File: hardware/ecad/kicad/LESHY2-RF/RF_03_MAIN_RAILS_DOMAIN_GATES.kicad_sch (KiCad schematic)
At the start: 0 parts

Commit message: complete exact H2.3.1 RF power hierarchy
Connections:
- no-connect marks 0 -> 20
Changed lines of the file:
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@@
 	(generator_version "10.0")
 	(paper "A4")
+	(hierarchical_label "3V3_MAIN"
+		(shape bidirectional)
+		(at 20.32 20.32 0)
+		(effects (font (size 1.27 1.27)))
+	)
+	(wire
+		(pts (xy 20.32 20.32) (xy 25.40 20.32))
+		(stroke (width 0) (type default))
+	)
+	(no_connect (at 25.40 20.32)
+	)
+	(hierarchical_label "5V_EXT_PREPROTECT"
+		(shape bidirectional)
+		(at 20.32 25.40 0)
+		(effects (font (size 1.27 1.27)))
+	)
+	(wire
+		(pts (xy 20.32 25.40) (xy 25.40 25.40))
+		(stroke (width 0) (type default))
+	)
+	(no_connect (at 25.40 25.40)
+	)
+	(hierarchical_label "5V_U214_PROTECTED"
+		(shape bidirectional)
+		(at 20.32 30.48 0)
+		(effects (font (size 1.27 1.27)))
+	)
+	(wire
+		(pts (xy 20.32 30.48) (xy 25.40 30.48))
+		(stroke (width 0) (type default))
+	)
+	(no_connect (at 25.40 30.48)
+	)
+	(hierarchical_label "AON_BUCK_EN"
+		(shape bidirectional)
+		(at 20.32 35.56 0)
+		(effects (font (size 1.27 1.27)))
+	)
+	(wire
+		(pts (xy 20.32 35.56) (xy 25.40 35.56))
+		(stroke (width 0) (type default))
+	)
+	(no_connect (at 25.40 35.56)
+	)
+	(hierarchical_label "AON_PG_N"
+		(shape bidirectional)
+		(at 20.32 40.64 0)
+		(effects (font (size 1.27 1.27)))
+	)
+	(wire
+		(pts (xy 20.32 40.64) (xy 25.40 40.64))
+		(stroke (width 0) (type default))
+	)
+	(no_connect (at 25.40 40.64)
+	)
+	(hierarchical_label "AON_SAFE_3V3"
+		(shape bidirectional)
+		(at 20.32 45.72 0)
+		(effects (font (size 1.27 1.27)))
+	)
+	(wire
+		(pts (xy 20.32 45.72) (xy 25.40 45.72))
+		(stroke (width 0) (type default))
+	)
+	(no_connect (at 25.40 45.72)
+	)
+	(hierarchical_label "EV_N8_LORA_EXT"
+		(shape bidirectional)
+		(at 20.32 50.80 0)
+		(effects (font (size 1.27 1.27)))
+	)
+	(wire
+		(pts (xy 20.32 50.80) (xy 25.40 50.80))
+		(stroke (width 0) (type default))
+	)
+	(no_connect (at 25.40 50.80)
+	)
+	(hierarchical_label "EXT_ANY_5V_EN_SAFE"
+		(shape bidirectional)
+		(at 20.32 55.88 0)
+		(effects (font (size 1.27 1.27)))
+	)
+	(wire
+		(pts (xy 20.32 55.88) (xy 25.40 55.88))
+		(stroke (width 0) (type default))
+	)
+	(no_connect (at 25.40 55.88)
+	)
+	(hierarchical_label "EXT_ANY_5V_REQ"
+		(shape bidirectional)
+		(at 20.32 60.96 0)
+		(effects (font (size 1.27 1.27)))
+	)
+	(wire
+		(pts (xy 20.32 60.96) (xy 25.40 60.96))
+		(stroke (width 0) (type default))
+	)
+	(no_connect (at 25.40 60.96)
+	)
+	(hierarchical_label "NVDC_SYS"
+		(shape bidirectional)
+		(at 20.32 66.04 0)
+		(effects (font (size 1.27 1.27)))
+	)
+	(wire
+		(pts (xy 20.32 66.04) (xy 25.40 66.04))
+		(stroke (width 0) (type default))
+	)
+	(no_connect (at 25.40 66.04)
+	)
+	(hierarchical_label "POR_N"
+		(shape bidirectional)
+		(at 190.50 20.32 180)
+		(effects (font (size 1.27 1.27)) (justify right))
+	)
+	(wire
+		(pts (xy 190.50 20.32) (xy 185.42 20.32))
+		(stroke (width 0) (type default))
+	)
+	(no_connect (at 185.42 20.32)
+	)
+	(hierarchical_label "POWER_GROUND"
+		(shape bidirectional)
+		(at 190.50 25.40 180)
+		(effects (font (size 1.27 1.27)) (justify right))
+	)
+	(wire
+		(pts (xy 190.50 25.40) (xy 185.42 25.40))
+		(stroke (width 0) (type default))
+	)
+	(no_connect (at 185.42 25.40)
+	)
+	(hierarchical_label "POWER_ZONE_TEMP_ADC"
+		(shape bidirectional)
+		(at 190.50 30.48 180)
+		(effects (font (size 1.27 1.27)) (justify right))
+	)
+	(wire
+		(pts (xy 190.50 30.48) (xy 185.42 30.48))
+		(stroke (width 0) (type default))
+	)
+	(no_connect (at 185.42 30.48)
+	)
+	(hierarchical_label "RF_ZONE_TEMP_ADC"
+		(shape bidirectional)
+		(at 190.50 35.56 180)
+		(effects (font (size 1.27 1.27)) (justify right))
+	)
+	(wire
+		(pts (xy 190.50 35.56) (xy 185.42 35.56))
+		(stroke (width 0) (type default))
+	)
+	(no_connect (at 185.42 35.56)
+	)
+	(hierarchical_label "SAFETY_GROUND"
+		(shape bidirectional)
+		(at 190.50 40.64 180)
+		(effects (font (size 1.27 1.27)) (justify right))
+	)
+	(wire
+		(pts (xy 190.50 40.64) (xy 185.42 40.64))
+		(stroke (width 0) (type default))
+	)
+	(no_connect (at 185.42 40.64)
+	)
+	(hierarchical_label "U214_5V_EN_SAFE"
+		(shape bidirectional)
+		(at 190.50 45.72 180)
+		(effects (font (size 1.27 1.27)) (justify right))
+	)
+	(wire
+		(pts (xy 190.50 45.72) (xy 185.42 45.72))
+		(stroke (width 0) (type default))
+	)
+	(no_connect (at 185.42 45.72)
+	)
+	(hierarchical_label "U214_5V_REQ"
+		(shape bidirectional)
+		(at 190.50 50.80 180)
+		(effects (font (size 1.27 1.27)) (justify right))
+	)
+	(wire
+		(pts (xy 190.50 50.80) (xy 185.42 50.80))
+		(stroke (width 0) (type default))
+	)
+	(no_connect (at 185.42 50.80)
+	)
+	(hierarchical_label "U214_PIN5_PROFILE"
+		(shape bidirectional)
+		(at 190.50 55.88 180)
+		(effects (font (size 1.27 1.27)) (justify right))
+	)
+	(wire
+		(pts (xy 190.50 55.88) (xy 185.42 55.88))
+		(stroke (width 0) (type default))
+	)
+	(no_connect (at 185.42 55.88)
+	)
+	(hierarchical_label "UNIT_5V_EN_SAFE"
+		(shape bidirectional)
+		(at 190.50 60.96 180)
+		(effects (font (size 1.27 1.27)) (justify right))
+	)
+	(wire
+		(pts (xy 190.50 60.96) (xy 185.42 60.96))
+		(stroke (width 0) (type default))
+	)
+	(no_connect (at 185.42 60.96)
+	)
+	(hierarchical_label "UNIT_5V_REQ"
+		(shape bidirectional)
+		(at 190.50 66.04 180)
+		(effects (font (size 1.27 1.27)) (justify right))
+	)
+	(wire
+		(pts (xy 190.50 66.04) (xy 185.42 66.04))
+		(stroke (width 0) (type default))
+	)
+	(no_connect (at 185.42 66.04)
+	)
 	(sheet_instances
 		(path "/"

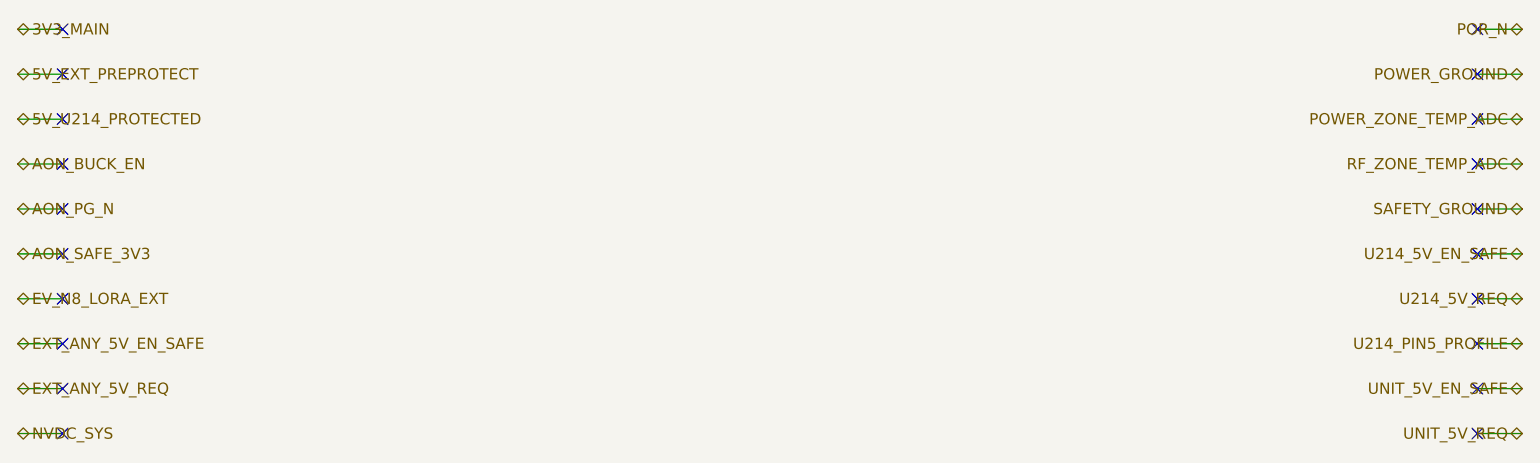
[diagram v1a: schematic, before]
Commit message: complete exact H2.3.2 USB PD charging
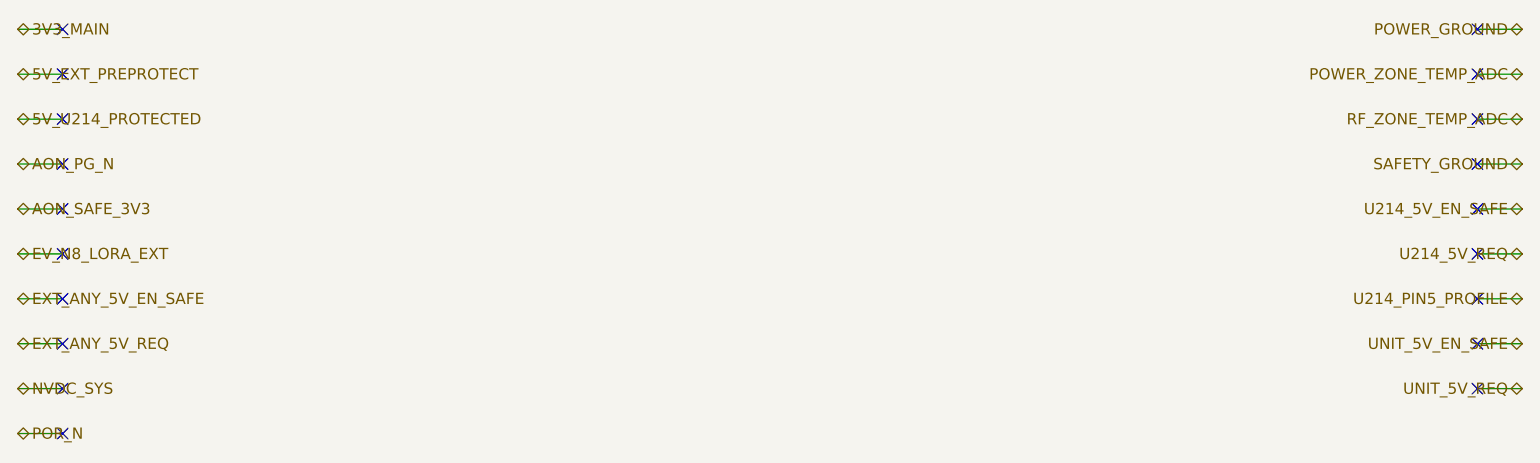
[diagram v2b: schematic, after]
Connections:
- no-connect marks 20 -> 19
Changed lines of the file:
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@@
 	(no_connect (at 25.40 30.48)
 	)
-	(hierarchical_label "AON_BUCK_EN"
+	(hierarchical_label "AON_PG_N"
 		(shape bidirectional)
 		(at 20.32 35.56 0)
@@
 	(no_connect (at 25.40 35.56)
 	)
-	(hierarchical_label "AON_PG_N"
+	(hierarchical_label "AON_SAFE_3V3"
 		(shape bidirectional)
 		(at 20.32 40.64 0)
@@
 	(no_connect (at 25.40 40.64)
 	)
-	(hierarchical_label "AON_SAFE_3V3"
+	(hierarchical_label "EV_N8_LORA_EXT"
 		(shape bidirectional)
 		(at 20.32 45.72 0)
@@
 	(no_connect (at 25.40 45.72)
 	)
-	(hierarchical_label "EV_N8_LORA_EXT"
+	(hierarchical_label "EXT_ANY_5V_EN_SAFE"
 		(shape bidirectional)
 		(at 20.32 50.80 0)
@@
 	(no_connect (at 25.40 50.80)
 	)
-	(hierarchical_label "EXT_ANY_5V_EN_SAFE"
+	(hierarchical_label "EXT_ANY_5V_REQ"
 		(shape bidirectional)
 		(at 20.32 55.88 0)
@@
 	(no_connect (at 25.40 55.88)
 	)
-	(hierarchical_label "EXT_ANY_5V_REQ"
+	(hierarchical_label "NVDC_SYS"
 		(shape bidirectional)
 		(at 20.32 60.96 0)
@@
 	(no_connect (at 25.40 60.96)
 	)
-	(hierarchical_label "NVDC_SYS"
+	(hierarchical_label "POR_N"
 		(shape bidirectional)
 		(at 20.32 66.04 0)
@@
 	(no_connect (at 25.40 66.04)
 	)
-	(hierarchical_label "POR_N"
+	(hierarchical_label "POWER_GROUND"
 		(shape bidirectional)
 		(at 190.50 20.32 180)
@@
 	(no_connect (at 185.42 20.32)
 	)
-	(hierarchical_label "POWER_GROUND"
+	(hierarchical_label "POWER_ZONE_TEMP_ADC"
 		(shape bidirectional)
 		(at 190.50 25.40 180)
@@
 	(no_connect (at 185.42 25.40)
 	)
-	(hierarchical_label "POWER_ZONE_TEMP_ADC"
+	(hierarchical_label "RF_ZONE_TEMP_ADC"
 		(shape bidirectional)
 		(at 190.50 30.48 180)
@@
 	(no_connect (at 185.42 30.48)
 	)
-	(hierarchical_label "RF_ZONE_TEMP_ADC"
+	(hierarchical_label "SAFETY_GROUND"
 		(shape bidirectional)
 		(at 190.50 35.56 180)
@@
 	(no_connect (at 185.42 35.56)
 	)
-	(hierarchical_label "SAFETY_GROUND"
+	(hierarchical_label "U214_5V_EN_SAFE"
 		(shape bidirectional)
 		(at 190.50 40.64 180)
@@
 	(no_connect (at 185.42 40.64)
 	)
-	(hierarchical_label "U214_5V_EN_SAFE"
+	(hierarchical_label "U214_5V_REQ"
 		(shape bidirectional)
 		(at 190.50 45.72 180)
@@
 	(no_connect (at 185.42 45.72)
 	)
-	(hierarchical_label "U214_5V_REQ"
+	(hierarchical_label "U214_PIN5_PROFILE"
 		(shape bidirectional)
 		(at 190.50 50.80 180)
@@
 	(no_connect (at 185.42 50.80)
 	)
-	(hierarchical_label "U214_PIN5_PROFILE"
+	(hierarchical_label "UNIT_5V_EN_SAFE"
 		(shape bidirectional)
 		(at 190.50 55.88 180)
@@
 	(no_connect (at 185.42 55.88)
 	)
-	(hierarchical_label "UNIT_5V_EN_SAFE"
+	(hierarchical_label "UNIT_5V_REQ"
 		(shape bidirectional)
 		(at 190.50 60.96 180)
@@
 	(no_connect (at 185.42 60.96)
 	)
-	(hierarchical_label "UNIT_5V_REQ"
-		(shape bidirectional)
-		(at 190.50 66.04 180)
-		(effects (font (size 1.27 1.27)) (justify right))
-	)
-	(wire
-		(pts (xy 190.50 66.04) (xy 185.42 66.04))
-		(stroke (width 0) (type default))
-	)
-	(no_connect (at 185.42 66.04)
-	)
 	(sheet_instances

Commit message: complete exact H2.3.4 power rails
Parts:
- added C1: TDK C1005X7R1H104K050BB, Capacitor_SMD:C_0402_1005Metric, symbol Leshy2:RF03_EXT_REQUEST_OR_BYPASS
- added C10: Murata GRM32ER71E226KE15L, Capacitor_SMD:C_1210_3225Metric, symbol Leshy2:RF03_MAIN_OUTPUT_CAP0
- added C11: Murata GRM32ER71E226KE15L, Capacitor_SMD:C_1210_3225Metric, symbol Leshy2:RF03_MAIN_OUTPUT_CAP1
- added C12: Murata GRM155R71H472KA01D, Capacitor_SMD:C_0402_1005Metric, symbol Leshy2:RF03_MAIN_EFUSE_DVDT_CAP
- added C13: Murata GRM1555C1H121JA01D, Capacitor_SMD:C_0402_1005Metric, symbol Leshy2:RF03_MAIN_EFUSE_ITIMER_CAP
- added C14: Murata GRM188R60J106ME47D, Capacitor_SMD:C_0603_1608Metric, symbol Leshy2:RF03_MAIN_EFUSE_OUTPUT_CAP
- added C15: Murata GRM32ER71E226KE15L, Capacitor_SMD:C_1210_3225Metric, symbol Leshy2:RF03_EXT_BUCK_INPUT_CAP
- added C16: TDK C1005X7R1H104K050BB, Capacitor_SMD:C_0402_1005Metric, symbol Leshy2:RF03_EXT_BUCK_HF_INPUT_CAP
- added C17: KEMET C0402C330J5GACTU, Capacitor_SMD:C_0402_1005Metric, symbol Leshy2:RF03_EXT_BUCK_FF_CAP
- added C18: Murata GRM32ER71E226KE15L, Capacitor_SMD:C_1210_3225Metric, symbol Leshy2:RF03_EXT_BUCK_OUTPUT_CAP0
- added C19: Murata GRM32ER71E226KE15L, Capacitor_SMD:C_1210_3225Metric, symbol Leshy2:RF03_EXT_BUCK_OUTPUT_CAP1
- added C2: TDK C1005X7R1H104K050BB, Capacitor_SMD:C_0402_1005Metric, symbol Leshy2:RF03_EXT_BRANCH_GATE_BYPASS
- added C20: Murata GRM155R71H472KA01D, Capacitor_SMD:C_0402_1005Metric, symbol Leshy2:RF03_EXT_DVDT_CAP
- added C21: Murata GRM188R71E224KA88D, Capacitor_SMD:C_0603_1608Metric, symbol Leshy2:RF03_EXT_ITIMER_CAP
- added C22: Murata GRM21BR71E225KE11L, Capacitor_SMD:C_0805_2012Metric, symbol Leshy2:RF03_EXT_INPUT_CAP
- added C23: Murata GRM21BR71E225KE11L, Capacitor_SMD:C_0805_2012Metric, symbol Leshy2:RF03_EXT_OUTPUT_CAP
- added C24: TDK C1005X7R1H104K050BB, Capacitor_SMD:C_0402_1005Metric, symbol Leshy2:RF03_POWER_ZONE_TEMP_FILTER
- added C25: TDK C1005X7R1H104K050BB, Capacitor_SMD:C_0402_1005Metric, symbol Leshy2:RF03_RF_ZONE_TEMP_FILTER
- added C26: TDK C1005X7R1H104K050BB, Capacitor_SMD:C_0402_1005Metric, symbol Leshy2:RF03_EXT_EVIDENCE_BUFFER_BYPASS
- added C3: TDK CGA5L1X7R1E475K160AC, Capacitor_SMD:C_1206_3216Metric, symbol Leshy2:RF03_AON_INPUT_CAP
- added C4: Murata GRM31CR71A226KE15L, Capacitor_SMD:C_1206_3216Metric, symbol Leshy2:RF03_AON_OUTPUT_CAP
- added C5: TDK C1005X7R1H104K050BB, Capacitor_SMD:C_0402_1005Metric, symbol Leshy2:RF03_AON_EFUSE_INPUT_CAP
- added C6: Murata GRM188R60J106ME47D, Capacitor_SMD:C_0603_1608Metric, symbol Leshy2:RF03_AON_EFUSE_OUTPUT_CAP
- added C7: Murata GRM32ER71E226KE15L, Capacitor_SMD:C_1210_3225Metric, symbol Leshy2:RF03_MAIN_INPUT_CAP
- added C8: TDK C1005X7R1H104K050BB, Capacitor_SMD:C_0402_1005Metric, symbol Leshy2:RF03_MAIN_HF_INPUT_CAP
- added C9: KEMET C0402C330J5GACTU, Capacitor_SMD:C_0402_1005Metric, symbol Leshy2:RF03_MAIN_FF_CAP
- added L1: Sunlord WPN201612H2R2MT, Inductor_SMD:L_Murata_LQH2MCNxxxx02_2.0x1.6mm, symbol Leshy2:RF03_AON_INDUCTOR
- added L2: Sunlord MWSA0503S-3R3MT, Inductor_SMD:L_Sunlord_MWSA0503S, symbol Leshy2:RF03_MAIN_INDUCTOR
- added L3: Sunlord MWSA0503S-4R7MT, Inductor_SMD:L_Sunlord_MWSA0503S, symbol Leshy2:RF03_EXT_INDUCTOR
- added Q1: Diodes Incorporated MMBT3904-7-F, Package_TO_SOT_SMD:SOT-23, symbol Leshy2:RF03_EXT_PG_QUALIFIER
- added R1: Yageo RC0402FR-0710KL, Resistor_SMD:R_0402_1005Metric, symbol Leshy2:RF03_EXT_ANY_REQ_PULLDOWN
- added R10: Yageo RT0402BRD07191KL, Resistor_SMD:R_0402_1005Metric, symbol Leshy2:RF03_MAIN_EFUSE_OVLO_TOP
- added R11: Yageo RT0402BRD07100KL, Resistor_SMD:R_0402_1005Metric, symbol Leshy2:RF03_MAIN_EFUSE_OVLO_BOTTOM
- added R12: Yageo RC0402FR-0745K3L, Resistor_SMD:R_0402_1005Metric, symbol Leshy2:RF03_MAIN_EFUSE_PG_TOP
- added R13: Yageo RC0402FR-0730KL, Resistor_SMD:R_0402_1005Metric, symbol Leshy2:RF03_MAIN_EFUSE_PG_BOTTOM
- added R14: Yageo RC0402FR-07100KL, Resistor_SMD:R_0402_1005Metric, symbol Leshy2:RF03_MAIN_EN_PULLDOWN
- added R15: Yageo RC0402FR-07220KL, Resistor_SMD:R_0402_1005Metric, symbol Leshy2:RF03_EXT_BUCK_FB_TOP
- added R16: Yageo RC0402FR-0730KL, Resistor_SMD:R_0402_1005Metric, symbol Leshy2:RF03_EXT_BUCK_FB_BOTTOM
- added R17: Yageo RC0402FR-0710KL, Resistor_SMD:R_0402_1005Metric, symbol Leshy2:RF03_EXT_EN_PULLDOWN
- added R18: Yageo RC0402FR-0710KL, Resistor_SMD:R_0402_1005Metric, symbol Leshy2:RF03_EXT_PG_PULLUP
- added R19: Yageo RC0402FR-0768KL, Resistor_SMD:R_0402_1005Metric, symbol Leshy2:RF03_EXT_PG_BASE_RES
- added R2: Yageo RC0402FR-0742K2L, Resistor_SMD:R_0402_1005Metric, symbol Leshy2:RF03_AON_MODE_RES
- added R20: Yageo RC0402FR-072K21L, Resistor_SMD:R_0402_1005Metric, symbol Leshy2:RF03_EXT_RILM
- added R21: Yageo RC0402FR-07169KL, Resistor_SMD:R_0402_1005Metric, symbol Leshy2:RF03_EXT_OVLO_TOP
- added R22: Yageo RC0402FR-0747KL, Resistor_SMD:R_0402_1005Metric, symbol Leshy2:RF03_EXT_OVLO_BOTTOM
- added R23: Yageo RC0603FR-071KL, Resistor_SMD:R_0603_1608Metric, symbol Leshy2:RF03_EXT_BLEEDER
- added R24: Yageo RC0402FR-0710KL, Resistor_SMD:R_0402_1005Metric, symbol Leshy2:RF03_POWER_ZONE_TEMP_PULLUP
- added R25: Yageo RC0402FR-0710KL, Resistor_SMD:R_0402_1005Metric, symbol Leshy2:RF03_RF_ZONE_TEMP_PULLUP
- added R26: Yageo RC0402FR-071KL, Resistor_SMD:R_0402_1005Metric, symbol Leshy2:RF03_EXT_EVIDENCE_INPUT_SERIES
- added R27: Yageo RC0402FR-0710KL, Resistor_SMD:R_0402_1005Metric, symbol Leshy2:RF03_EXT_EVIDENCE_INPUT_PULLUP
- added R28: Yageo RC0402FR-0710KL, Resistor_SMD:R_0402_1005Metric, symbol Leshy2:RF03_EXT_EVIDENCE_OUTPUT_PULLUP
- added R3: Yageo RC0402FR-07240KL, Resistor_SMD:R_0402_1005Metric, symbol Leshy2:RF03_AON_EFUSE_RILIM
- added R4: Yageo RC0402FR-07196KL, Resistor_SMD:R_0402_1005Metric, symbol Leshy2:RF03_AON_EFUSE_OVLO_TOP
- added R5: Yageo RC0402FR-07100KL, Resistor_SMD:R_0402_1005Metric, symbol Leshy2:RF03_AON_EFUSE_OVLO_BOTTOM
- added R6: Yageo RC0402FR-0747KL, Resistor_SMD:R_0402_1005Metric, symbol Leshy2:RF03_AON_PG_PULLUP
- added R7: Yageo RC0402FR-0745K3L, Resistor_SMD:R_0402_1005Metric, symbol Leshy2:RF03_MAIN_FB_TOP
- added R8: Yageo RC0402FR-0710KL, Resistor_SMD:R_0402_1005Metric, symbol Leshy2:RF03_MAIN_FB_BOTTOM
- added R9: Yageo RC0402FR-071K65L, Resistor_SMD:R_0402_1005Metric, symbol Leshy2:RF03_MAIN_EFUSE_RILM
- added RT1: TDK B57332V5103F360, Resistor_SMD:R_0603_1608Metric, symbol Leshy2:RF03_POWER_ZONE_NTC
- added RT2: TDK B57332V5103F360, Resistor_SMD:R_0603_1608Metric, symbol Leshy2:RF03_RF_ZONE_NTC
- added U1: 74LVC1G32GV,125, Package_TO_SOT_SMD:SC-74A-5_1.55x2.9mm_P0.95mm, symbol Leshy2:RF03_EXT_REQUEST_OR
- added U2: Texas Instruments SN74LVC2G08DCUR, Package_SO:VSSOP-8_2.3x2mm_P0.5mm, symbol Leshy2:RF03_EXT_BRANCH_GATE
- added U3: Texas Instruments TPS629203DRLR, Leshy2:TI-DRL0008A-SOT-5X3-8, symbol Leshy2:RF03_AON_BUCK
- added U4: Texas Instruments TPS25961DRVR, Package_SON:WSON-6-1EP_2x2mm_P0.65mm_EP1x1.6mm, symbol Leshy2:RF03_AON_EFUSE
- added U5: Texas Instruments TPS564252DRLR, Package_TO_SOT_SMD:Texas_R-PDSO-N6_DRL-6, symbol Leshy2:RF03_MAIN_BUCK
- added U6: Texas Instruments TPS25974LRPWR, Leshy2:TI-RPW0010A-VQFN-HR-10, symbol Leshy2:RF03_MAIN_EFUSE
- added U7: Texas Instruments TPS564252DRLR, Package_TO_SOT_SMD:Texas_R-PDSO-N6_DRL-6, symbol Leshy2:RF03_EXT_BUCK
- added U8: Texas Instruments TPS259470LRPWR, Leshy2:TI-RPW0010A-VQFN-HR-10, symbol Leshy2:RF03_EXT_EFUSE
- added U9: SN74LVC1G07DCKR, Package_TO_SOT_SMD:Texas_R-PDSO-G5_DCK-5, symbol Leshy2:RF03_EXT_EVIDENCE_BUFFER
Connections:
- net 3V3_MAIN: now also C14.1 (END_1), R12.1 (END_1), R18.1 (END_1), U6.6 (OUT)
- net 5V_EXT_PREPROTECT: now also C17.1 (END_1), C18.1 (END_1), C19.1 (END_1), C22.1 (END_1), L3.2 (END_2), R15.1 (END_1), R21.1 (END_1), U8.5 (IN)
- net 5V_U214_PROTECTED: now also C23.1 (END_1), R23.1 (END_1), U8.6 (OUT)
- net AON_PG_N: now also R6.2 (END_2), U3.2 (PG)
- net AON_SAFE_3V3: now also C1.1 (END_1), C2.1 (END_1), C26.1 (END_1), C6.1 (END_1), R24.1 (END_1), R25.1 (END_1), R27.1 (END_1), R28.1 (END_1), R6.1 (END_1), U1.5 (VCC), U2.8 (VCC), U4.1 (OUT), U9.5 (VCC)
- net EV_N8_LORA_EXT: now also R28.2 (END_2), U9.4 (Y)
- net EXT_ANY_5V_EN_SAFE: now also R17.1 (END_1), R19.1 (END_1), U2.2 (1B), U2.6 (2B), U7.5 (EN)
- net EXT_ANY_5V_REQ: now also R1.1 (END_1), U1.4 (1Y)
- net NVDC_SYS: now also C15.1 (END_1), C16.1 (END_1), C3.1 (END_1), C7.1 (END_1), C8.1 (END_1), U3.6 (VIN), U3.7 (EN), U5.1 (VIN), U7.1 (VIN)
- net POR_N: now also R14.1 (END_1), U5.5 (EN)
- net POWER_GROUND: now also C10.2 (END_2), C11.2 (END_2), C12.2 (END_2), C13.2 (END_2), C14.2 (END_2), C15.2 (END_2), C16.2 (END_2), C18.2 (END_2), C19.2 (END_2), C20.2 (END_2), C21.2 (END_2), C22.2 (END_2), C23.2 (END_2), C3.2 (END_2), C4.2 (END_2), C5.2 (END_2), C6.2 (END_2), C7.2 (END_2), C8.2 (END_2), R11.2 (END_2), R13.2 (END_2), R14.2 (END_2), R16.2 (END_2), R17.2 (END_2), R2.2 (END_2), R20.2 (END_2), R22.2 (END_2), R23.2 (END_2), R3.2 (END_2), R5.2 (END_2), R8.2 (END_2), R9.2 (END_2), U3.5 (GND), U4.4 (GND), U4.7 (EP_GND), U5.3 (GND), U6.8 (GND), U7.3 (GND), U8.8 (GND)
- net POWER_ZONE_TEMP_ADC: now also C24.1 (END_1), R24.2 (END_2), RT1.1 (END_1)
- net RF_ZONE_TEMP_ADC: now also C25.1 (END_1), R25.2 (END_2), RT2.1 (END_1)
- net SAFETY_GROUND: now also C1.2 (END_2), C2.2 (END_2), C24.2 (END_2), C25.2 (END_2), C26.2 (END_2), R1.2 (END_2), RT1.2 (END_2), RT2.2 (END_2), U1.3 (GND), U2.4 (GND), U9.3 (GND)
- net U214_5V_EN_SAFE: now also U2.7 (1Y), U8.1 (EN_UVLO)
- net U214_5V_REQ: now also U1.1 (1A), U2.1 (1A)
- net U214_PIN5_PROFILE: now also R26.1 (END_1)
- net UNIT_5V_EN_SAFE: now also U2.3 (2Y)
- net UNIT_5V_REQ: now also U1.2 (1B), U2.5 (2A)
- new net AON_BUCK_SW: L1.1 (END_1), U3.4 (SW)
- new net AON_EFUSE_ILIM: R3.1 (END_1), U4.3 (ILIM)
- new net AON_EFUSE_OVLO: R4.2 (END_2), R5.1 (END_1), U4.2 (OVLO)
- new net AON_MODE_SET: R2.1 (END_1), U3.8 (MODE_SCONF)
- new net AON_RAW_3V3: C4.1 (END_1), C5.1 (END_1), L1.2 (END_2), R4.1 (END_1), U3.3 (VOS), U4.5 (EN_UVLO), U4.6 (IN)
- new net EXT_5V_FB: C17.2 (END_2), R15.2 (END_2), R16.1 (END_1), U7.6 (FB)
- new net EXT_5V_PG_N: Q1.2 (E), R18.2 (END_2), U7.4 (PG)
- new net EXT_BUCK_SW: L3.1 (END_1), U7.2 (SW)
- new net EXT_EFUSE_DVDT: C20.1 (END_1), U8.7 (DVDT)
- new net EXT_EFUSE_ITIMER: C21.1 (END_1), U8.10 (ITIMER)
- new net EXT_EFUSE_OVLO_SENSE: R21.2 (END_2), R22.1 (END_1), U8.2 (OVLO)
- new net EXT_PG_QUAL_BASE: Q1.1 (B), R19.2 (END_2)
- new net MAIN_3V3_FB: C9.2 (END_2), R7.2 (END_2), R8.1 (END_1), U5.6 (FB)
- new net MAIN_BUCK_SW: L2.1 (END_1), U5.2 (SW)
- new net MAIN_EFUSE_DVDT: C12.1 (END_1), U6.7 (DVDT)
- new net MAIN_EFUSE_ILM: R9.1 (END_1), U6.9 (ILM)
- new net MAIN_EFUSE_ITIMER: C13.1 (END_1), U6.10 (ITIMER)
- new net MAIN_EFUSE_OVLO: R10.2 (END_2), R11.1 (END_1), U6.2 (OVLO)
- new net MAIN_EFUSE_PGTH: R12.2 (END_2), R13.1 (END_1), U6.4 (PGTH)
- new net MAIN_RAW_3V3: C10.1 (END_1), C11.1 (END_1), C9.1 (END_1), L2.2 (END_2), R10.1 (END_1), R7.1 (END_1), U6.1 (EN_UVLO), U6.5 (IN)
- new net MAIN_RAW_3V3_PG_N: U5.4 (PG)
- new net POWER_FAULT_N: Q1.3 (C), U6.3 (PG), U8.4 (FLT)
- new net U214_5V_CURRENT_MONITOR: R20.1 (END_1), U8.9 (ILM)
- new net U214_PIN5_SENSE: R26.2 (END_2), R27.2 (END_2), U9.2 (A)
- no-connect marks 19 -> 3
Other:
- title: (none) -> Leshy2 — exact independent rails, eFuses and accessory gates

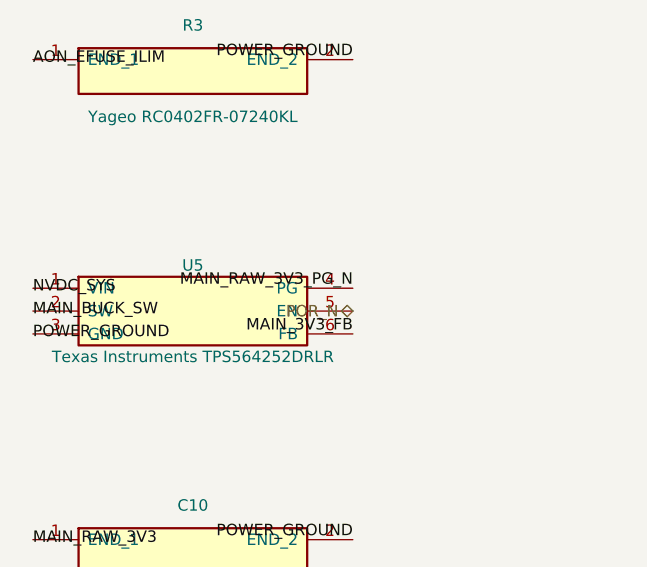
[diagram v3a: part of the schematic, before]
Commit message: complete exact H2.3.13 RF testpoint sheet
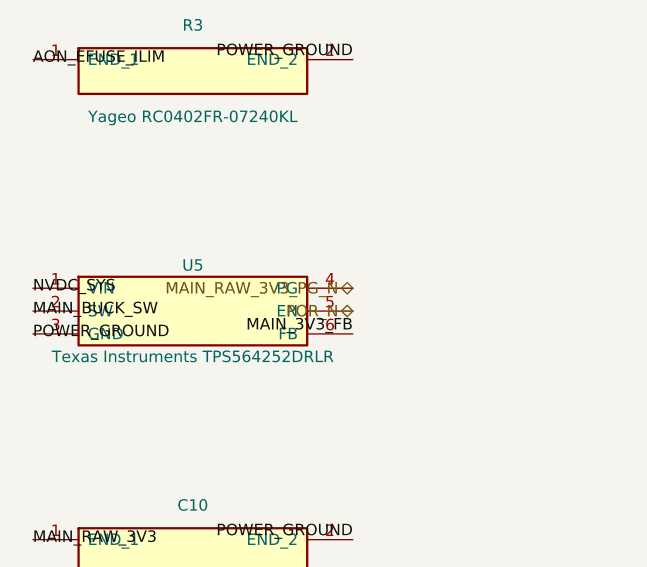
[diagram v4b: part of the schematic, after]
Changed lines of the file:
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@@
 		(effects (font (size 1.27 1.27)))
 	)
-	(label "MAIN_RAW_3V3_PG_N"
+	(hierarchical_label "MAIN_RAW_3V3_PG_N"
+		(shape bidirectional)
 		(at 68.58 96.52 180)
 		(effects (font (size 1.27 1.27)) (justify right bottom))

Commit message: complete H2 schematic review package
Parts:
- renumbered C1 to C3001, C2 to C3002, C3 to C3003, C4 to C3004, C5 to C3005, C6 to C3006, C7 to C3007, C8 to C3008, C9 to C3009, C10 to C3010, C11 to C3011, C12 to C3012, C13 to C3013, C14 to C3014, C15 to C3015, C16 to C3016, C17 to C3017, C18 to C3018, C19 to C3019, C20 to C3020, C21 to C3021, C22 to C3022, C23 to C3023, C24 to C3024, C25 to C3025, C26 to C3026, L1 to L3001, L2 to L3002, L3 to L3003, Q1 to Q3001, R1 to R3001, R2 to R3002, R3 to R3003, R4 to R3004, R5 to R3005, R6 to R3006, R7 to R3007, R8 to R3008, R9 to R3009, R10 to R3010, R11 to R3011, R12 to R3012, R13 to R3013, R14 to R3014, R15 to R3015, R16 to R3016, R17 to R3017, R18 to R3018, R19 to R3019, R20 to R3020, R21 to R3021, R22 to R3022, R23 to R3023, R24 to R3024, R25 to R3025, R26 to R3026, R27 to R3027, R28 to R3028, RT1 to RT3001, RT2 to RT3002, U1 to U3001, U2 to U3002, U3 to U3003, U4 to U3004, U5 to U3005, U6 to U3006, U7 to U3007, U8 to U3008, U9 to U3009

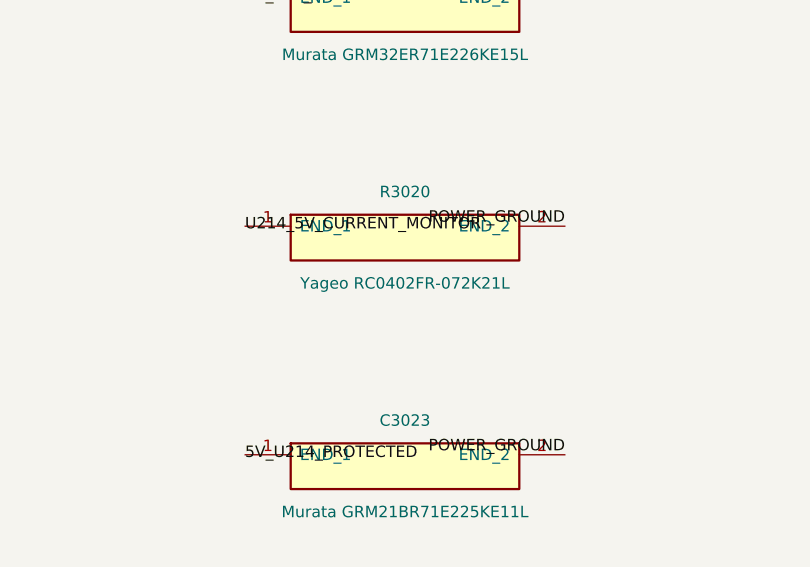
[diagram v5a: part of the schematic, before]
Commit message: docs: complete H3.1 steady power verification
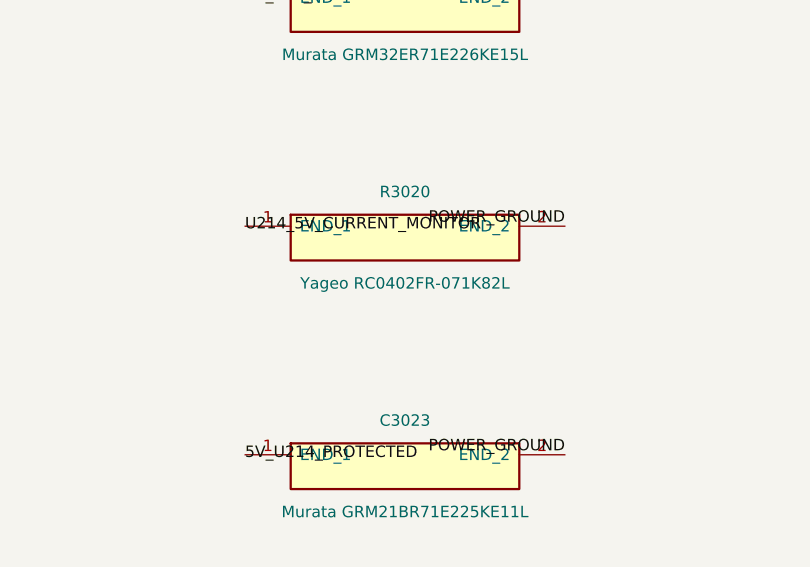
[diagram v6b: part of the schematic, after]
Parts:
- R3020: value Yageo RC0402FR-072K21L -> Yageo RC0402FR-071K82L
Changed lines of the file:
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@@
 			(effects (font (size 1.27 1.27)))
 		)
-		(property "Value" "Yageo RC0402FR-072K21L"
+		(property "Value" "Yageo RC0402FR-071K82L"
 			(at 375.92 227.33 0)
 			(show_name no)
@@
 			(effects (font (size 1.27 1.27)))
 		)
-		(property "Description" "2_21kohm_1pct_0402_efuse_current_limit_resistor"
+		(property "Description" "1_82kohm_1pct_0402_efuse_current_limit_resistor"
 			(at 375.92 222.25 0)
 			(show_name no)

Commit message: Complete H3.3.1 display electrical verification
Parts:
- R3007: value Yageo RC0402FR-0745K3L -> Vishay TNPW040243K7BEED
- R3008: value Yageo RC0402FR-0710KL -> Vishay TNPW040210K0BEED
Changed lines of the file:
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@@
 			(effects (font (size 1.27 1.27)))
 		)
-		(property "Value" "Yageo RC0402FR-0745K3L"
+		(property "Value" "Vishay TNPW040243K7BEED"
 			(at 132.08 125.73 0)
 			(show_name no)
@@
 			(effects (font (size 1.27 1.27)))
 		)
-		(property "Description" "45_3kohm_1pct_0402_main_feedback_top_resistor"
+		(property "Description" "43_7kohm_0_1pct_25ppm_0402_main_feedback_top_resistor"
 			(at 132.08 120.65 0)
 			(show_name no)
@@
 			(effects (font (size 1.27 1.27)))
 		)
-		(property "Value" "Yageo RC0402FR-0710KL"
+		(property "Value" "Vishay TNPW040210K0BEED"
 			(at 213.36 125.73 0)
 			(show_name no)
@@
 			(effects (font (size 1.27 1.27)))
 		)
-		(property "Description" "10kohm_1pct_0402_main_feedback_bottom_resistor"
+		(property "Description" "10kohm_0_1pct_25ppm_0402_main_feedback_bottom_resistor"
 			(at 213.36 120.65 0)
 			(show_name no)
